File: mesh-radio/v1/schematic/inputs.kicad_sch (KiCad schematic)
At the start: 39 parts, among them J1 12401610E4#2A, J2 SM02B-SRSS-TB(LF)(SN), U1 TPS259470ARPWR, U2 TPS259470ARPWR, U3 TPS259470ARPWR

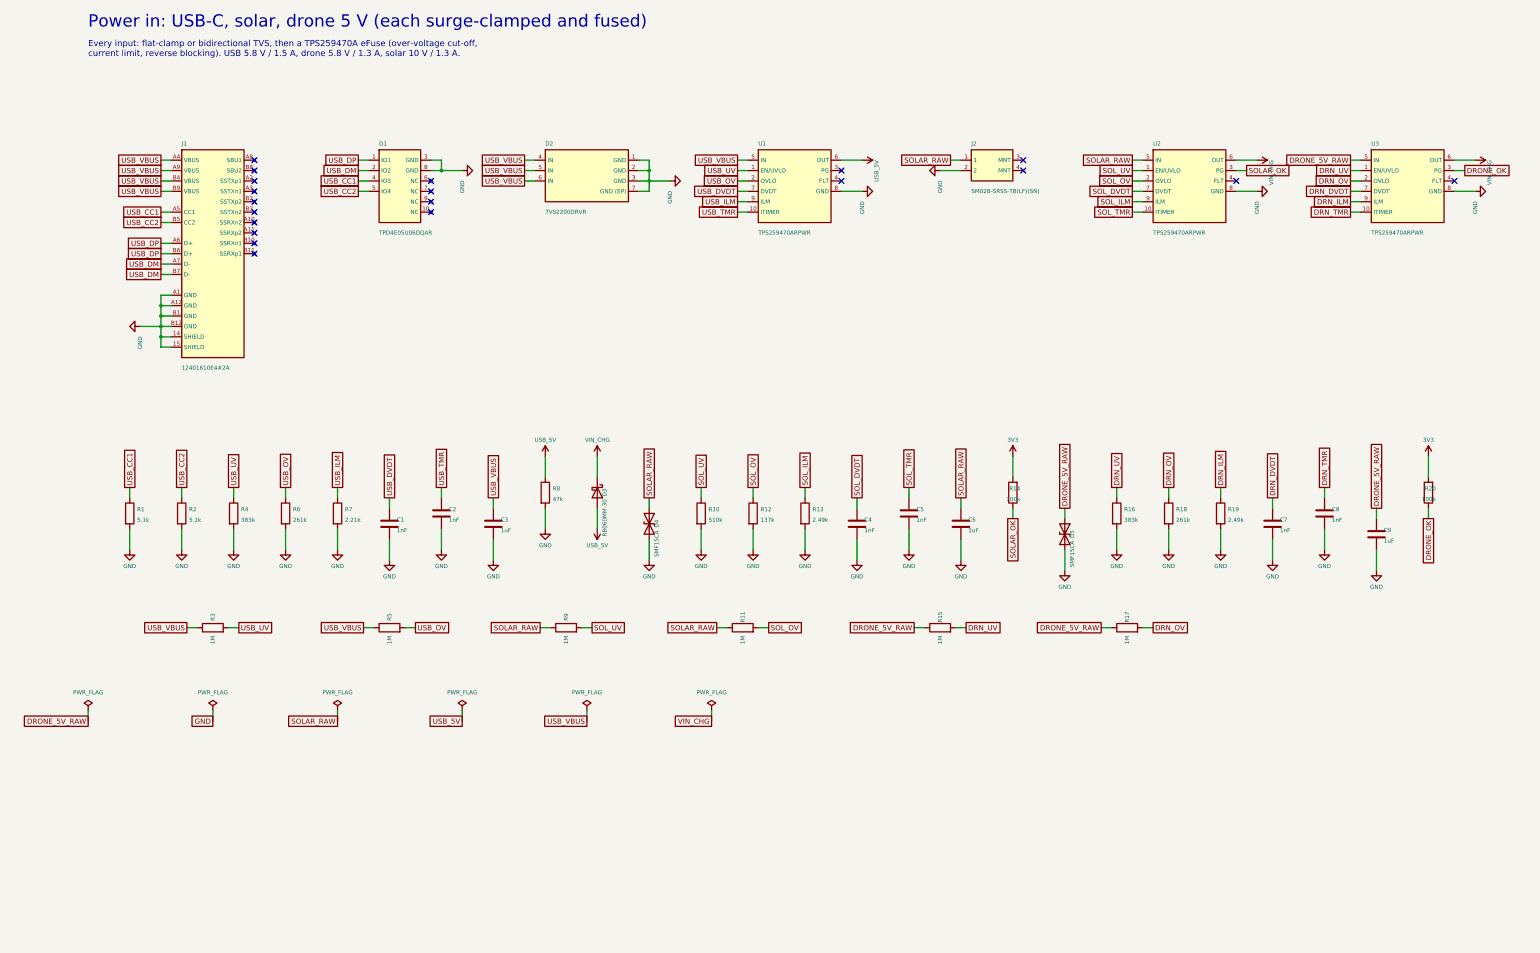
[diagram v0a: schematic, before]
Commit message: Mesh Radio v1: fix every design-review finding, add the part audit
An independent review of the schematic found two critical and nine further
issues; all are fixed in src/circuit.py:
- reverse-battery FET gate now returns to the cell's own minus terminal, so
  a backwards cell stays isolated even while USB/solar/drone power the board
- solar and drone inputs: reverse-blocking Schottky + 22 V flat-clamp TVS
  (the 15 V TVS would have failed on a 12 V panel); 4.7 V clamp on every
  eFuse EN/UVLO pin so 20 V on an input stays inside its rating
- ideal diode (LM66100) holds VSYS on the cell when a 3 W burst trips the
  charger's 3.0 V battery disconnect
- charge LED moved to STAT2 (charging), USB cut-off lowered to 5.4 V,
  charger /CE on a GPIO for firmware temperature control, -40 C TCXO,
  power mux on only with the amplifier, header VSYS pin removed
- firmware ceilings documented: SX1262 +20 dBm, amplifier 3.6 V by default

docs/part-audit.md: all 125 lines checked at DigiKey and LCSC (genuine
LCSC numbers, DigiKey numbers, second sources for out-of-stock lines);
parts cost about $76 at 10 boards, $58 at 100.

Schematic regenerated: ERC 0 violations, netlist equals circuit.py.

Co-Authored-By: Claude Opus 5.5 <noreply@anthropic.com>
Claude-Session: https://claude.ai/code/session_015TBB2ThqxHSgA8MkFosmn9
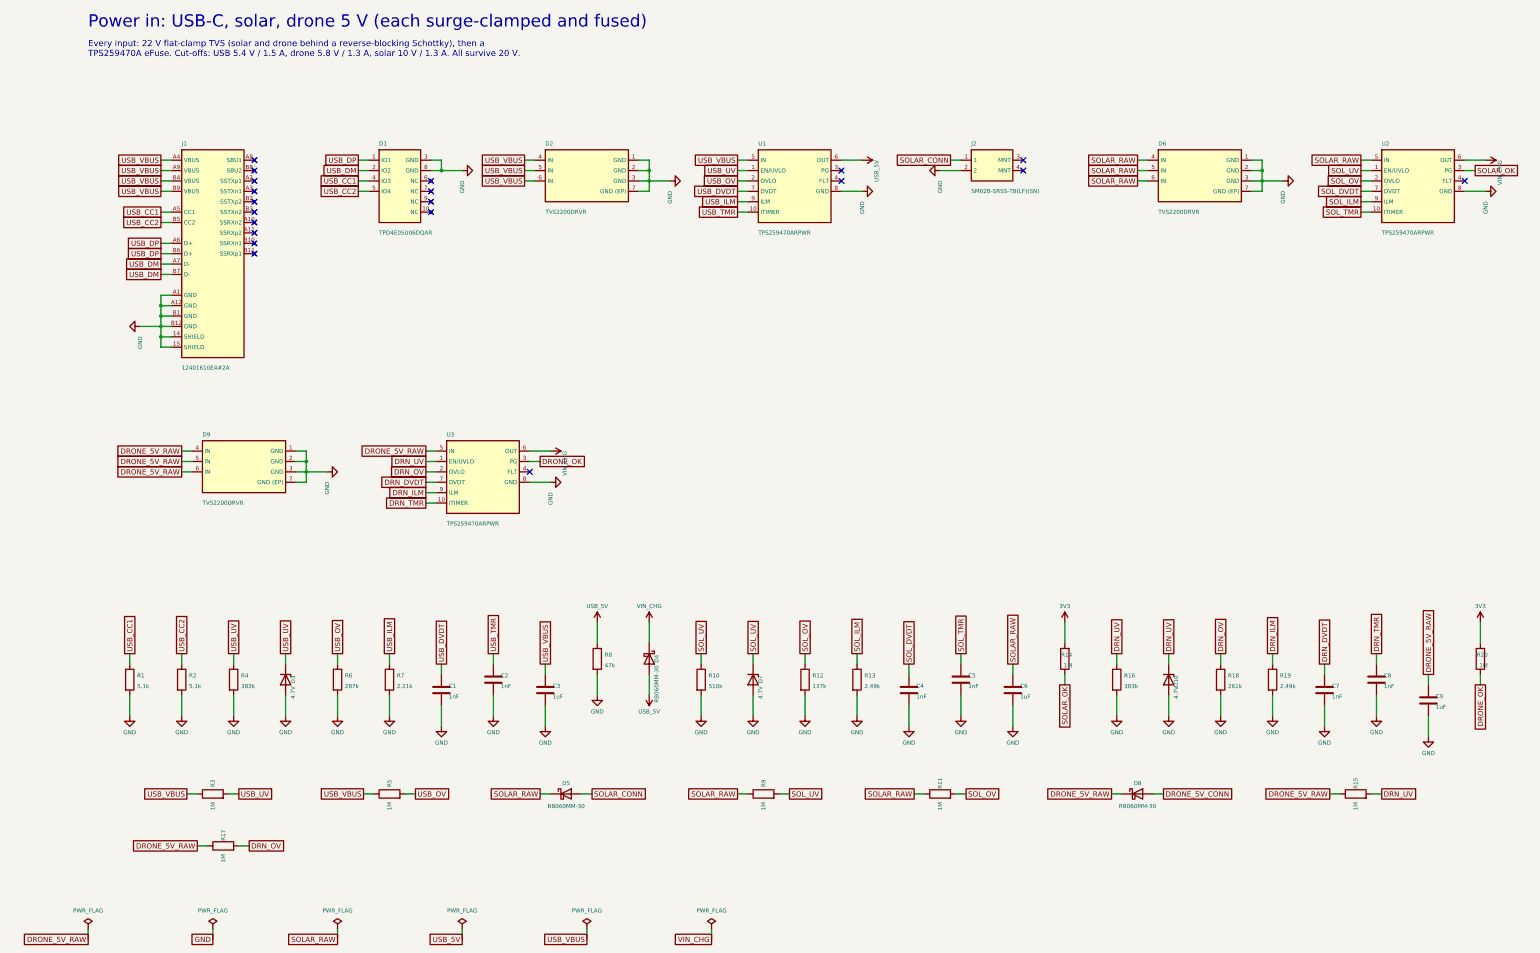
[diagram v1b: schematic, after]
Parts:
- added D10, D7: 4.7V, og:SOD-323FL, symbol og_device:D_Zener_ZENER4V7
- added D6, D9: TVS2200DRVR, og:WSON-6_L2.0-W2.0-P0.65-BL-EP, symbol og:TVS2200
- added D8: RB060MM-30, og:SOD-123FL, symbol og_device:D_Schottky_RB060MM
- C1, C2, C4, C5, C7, C8: DigiKey (none) -> 490-3244-1-ND
- C3, C6, C9: DigiKey (none) -> 1276-1184-1-ND
- D1: DigiKey (none) -> 296-35765-1-ND
- D2: DigiKey (none) -> 296-52187-1-ND
- D3: value RB060MM-30 -> 4.7V; footprint og:SOD-123FL -> og:SOD-323FL; symbol og_device:D_Schottky_RB060MM -> og_device:D_Zener_ZENER4V7; LCSC C308720 -> C209560; MPN RB060MM-30TR -> UDZVTE-174.7B
- D4, D5: value SMF15CA -> RB060MM-30; symbol og_device:D_TVS_SMF15CA -> og_device:D_Schottky_RB060MM; DigiKey (none) -> RB060MM-30CT-ND; LCSC C1851361 -> C308720; MPN SMF15CA -> RB060MM-30TR; Manufacturer Littelfuse -> Rohm
- J1: DigiKey (none) -> 12401610E4#2ACT-ND
- J2: DigiKey (none) -> 455-SM02B-SRSS-TBCT-ND
- R1, R2: DigiKey (none) -> 311-5.10KLRCT-ND
- R10: DigiKey (none) -> 311-510KLRCT-ND
- R11, R15, R17, R3, R5, R9: DigiKey (none) -> 311-1.00MLRCT-ND
- R12: DigiKey (none) -> YAG2972CT-ND
- R13, R19: DigiKey (none) -> 311-2.49KLRCT-ND
- R14, R20: value 100k -> 1M; DigiKey (none) -> 311-1.00MLRCT-ND; LCSC C60491 -> C138033; MPN RC0402FR-07100KL -> RC0402FR-071ML
- R16, R4: DigiKey (none) -> YAG3139CT-ND
- R18: DigiKey (none) -> 311-261KLRCT-ND
- R6: value 261k -> 287k; LCSC C185437 -> C327358; MPN RC0402FR-07261KL -> RC0402FR-07287KL
- R7: DigiKey (none) -> 311-2.21KLRCT-ND
- R8: DigiKey (none) -> 311-47.0KLRCT-ND
- U1, U2, U3: DigiKey (none) -> 296-TPS259470ARPWRCT-ND
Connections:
- net DRN_UV: now also D10.1 (K)
- net DRONE_5V_RAW: now also D8.1 (K), D9.4 (IN), D9.5 (IN), D9.6 (IN); no longer D5.1 (A1)
- net GND: now also D3.2 (A), D10.2 (A), D6.1 (GND), D6.2 (GND), D6.3 (GND), D6.7 (GND (EP)), D7.2 (A), D9.1 (GND), D9.2 (GND), D9.3 (GND), D9.7 (GND (EP)); no longer D4.2 (A2), D5.2 (A2)
- net SOLAR_RAW: now also D5.1 (K), D6.4 (IN), D6.5 (IN), D6.6 (IN); no longer D4.1 (A1), J2.1
- net SOL_UV: now also D7.1 (K)
- net USB_5V: now also D4.2 (A); no longer D3.2 (A)
- net USB_UV: now also D3.1 (K)
- net VIN_CHG: now also D4.1 (K); no longer D3.1 (K)
- new net DRONE_5V_CONN: D8.2 (A)
- new net SOLAR_CONN: D5.2 (A), J2.1
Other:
- note added: "Every input: 22 V flat-clamp TVS (solar and drone behind a reverse-blocking Schottky), then a TPS259470A eFuse. Cut-offs: USB 5.4 V / 1.5 A, drone 5.8 V / 1.3 A, solar 10 V / 1.3 A. All survive 20 V."
- note removed: "Every input: flat-clamp or bidirectional TVS, then a TPS259470A eFuse (over-voltage cut-off, current limit, reverse blocking). USB 5.8 V / 1.5 A, drone 5.8 V / 1.3 A, solar 10 V / 1.3 A."
- moved on the sheet: C1, C2, C3, C4, C5, C6, C7, C8, C9, D3, D4, D5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

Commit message: Mesh radio v1: power-path and firmware rework in progress (snapshot)
Co-Authored-By: Claude Opus 5.5 <noreply@anthropic.com>
Claude-Session: https://claude.ai/code/session_015TBB2ThqxHSgA8MkFosmn9
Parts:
- removed C9: 1uF, og:C_0603, symbol Device:C
- removed D10, D7: 4.7V, og:SOD-323FL, symbol og_device:D_Zener_ZENER4V7
- removed D8: RB060MM-30, og:SOD-123FL, symbol og_device:D_Schottky_RB060MM
- removed D9: TVS2200DRVR, og:WSON-6_L2.0-W2.0-P0.65-BL-EP, symbol og:TVS2200
- added R21: 1.5M, og:R_0402, symbol Device:R
- added R22: 100k, og:R_0402, symbol Device:R
- C1: value 1nF -> 100pF; DigiKey 490-3244-1-ND -> 490-5922-1-ND; LCSC C76947 -> C77177; MPN GRM1555C1H102JA01D -> GRM1555C1H101JA01D
- C3: value 1uF -> 1nF; footprint og:C_0603 -> og:C_0402; DigiKey 1276-1184-1-ND -> 490-3244-1-ND; LCSC C29936 -> C76947; MPN CL10B105KA8NNNC -> GRM1555C1H102JA01D; Manufacturer Samsung Electro-Mechanics -> Murata
- C4, C7, C8: value 1nF -> 1uF; footprint og:C_0402 -> og:C_0603; DigiKey 490-3244-1-ND -> 587-2400-1-ND; LCSC C76947 -> C92848; MPN GRM1555C1H102JA01D -> UMK107BJ105KA-T; Manufacturer Murata -> Taiyo Yuden
- C5: value 1nF -> 4.7uF; footprint og:C_0402 -> og:C_1206; DigiKey 490-3244-1-ND -> 1276-2789-1-ND; LCSC C76947 -> C51205; MPN GRM1555C1H102JA01D -> CL31B475KBHNNNE; Manufacturer Murata -> Samsung Electro-Mechanics
- C6: value 1uF -> 4.7uF; DigiKey 1276-1184-1-ND -> 1276-1044-1-ND; LCSC C29936 -> C1705; MPN CL10B105KA8NNNC -> CL10A475KP8NNNC
- D3: value 4.7V -> 5.6V; symbol og_device:D_Zener_ZENER4V7 -> og_device:D_Zener_ZENER5V6; DigiKey (none) -> UDZVTE-175.6BCT-ND; LCSC C209560 -> C79630; MPN UDZVTE-174.7B -> UDZVTE-175.6B
- D5: value RB060MM-30 -> SMF33CA; symbol og_device:D_Schottky_RB060MM -> Device:D_TVS; DigiKey RB060MM-30CT-ND -> 18-SMF33CACT-ND; LCSC C308720 -> C1851347; MPN RB060MM-30TR -> SMF33CA; Manufacturer Rohm -> Littelfuse
- D6: value TVS2200DRVR -> SMF33CA; footprint og:WSON-6_L2.0-W2.0-P0.65-BL-EP -> og:SOD-123FL; symbol og:TVS2200 -> Device:D_TVS; DigiKey 296-52187-1-ND -> 18-SMF33CACT-ND; LCSC C523793 -> C1851347; MPN TVS2200DRVR -> SMF33CA; Manufacturer Texas Instruments -> Littelfuse
- R10: value 510k -> 22R; DigiKey 311-510KLRCT-ND -> 311-22.0LRCT-ND; LCSC C137961 -> C114765; MPN RC0402FR-07510KL -> RC0402FR-0722RL
- R11, R15, R17: value 1M -> 1.5M; DigiKey 311-1.00MLRCT-ND -> 13-RC0402FR-071M5LCT-ND; LCSC C138033 -> C138034; MPN RC0402FR-071ML -> RC0402FR-071M5L
- R12: value 137k -> 267k; DigiKey YAG2972CT-ND -> YAG3079CT-ND; LCSC C138058 -> C327360; MPN RC0402FR-07137KL -> RC0402FR-07267KL
- R13, R19: value 2.49k -> 1M; DigiKey 311-2.49KLRCT-ND -> 311-1.00MLRCT-ND; LCSC C145071 -> C138033; MPN RC0402FR-072K49L -> RC0402FR-071ML
- R14, R20: value 1M -> 2.1k; DigiKey 311-1.00MLRCT-ND -> YAG3098CT-ND; LCSC C138033 -> C163473; MPN RC0402FR-071ML -> RC0402FR-072K1L
- R16: value 383k -> 100k; DigiKey YAG3139CT-ND -> 311-100KLRCT-ND; LCSC C163468 -> C60491; MPN RC0402FR-07383KL -> RC0402FR-07100KL
- R18: value 261k -> 267k; DigiKey 311-261KLRCT-ND -> YAG3079CT-ND; LCSC C185437 -> C327360; MPN RC0402FR-07261KL -> RC0402FR-07267KL
- R3: value 1M -> 20k; DigiKey 311-1.00MLRCT-ND -> 311-20.0KLRCT-ND; LCSC C138033 -> C93942; MPN RC0402FR-071ML -> RC0402FR-0720KL
- R4: value 383k -> 7.68k; DigiKey YAG3139CT-ND -> YAG3237CT-ND; LCSC C163468 -> C155695; MPN RC0402FR-07383KL -> RC0402FR-077K68L
- R8: value 47k -> 1R; footprint og:R_0402 -> og:R_0805; DigiKey 311-47.0KLRCT-ND -> 541-1.00TCT-ND; LCSC C93943 -> C313850; MPN RC0402FR-0747KL -> CRCW08051R00FKEAHP; Manufacturer Yageo -> Vishay Dale
- R9: value 1M -> 2.2k; DigiKey 311-1.00MLRCT-ND -> 311-2.20KLRCT-ND; LCSC C138033 -> C114762; MPN RC0402FR-071ML -> RC0402FR-072K2L
- U2, U3: value TPS259470ARPWR -> MAX17608ATC+T; footprint og:VQFN-10_L2.0-W2.0-P0.45-TL -> og:TDFN-12_L3.0-W3.0-P0.50-BL-EP; symbol og:TPS259470A -> og:MAX17608; DigiKey 296-TPS259470ARPWRCT-ND -> 175-MAX17608ATC+TCT-ND; LCSC C3662799 -> C2155884; MPN TPS259470ARPWR -> MAX17608ATC+T; Manufacturer Texas Instruments -> Analog Devices
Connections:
- net 3V3 is gone; now on net GND: R14.2, R20.2
- net DRN_OV: now also U3.3 (OVLO); no longer U3.2 (OVLO)
- net DRN_UV: now also R19.2, U3.4 (UVLO); no longer R15.2, R16.1, U3.1 (EN/UVLO)
- net DRONE_5V_CONN: now also C8.1, D6.1 (A1), R17.1, R19.1, U3.1 (IN), U3.2 (IN), R21.1
- net DRONE_OK: now also R21.2, R22.1; no longer R20.1, U3.3 (PG)
- net GND: now also D5.2 (A2), R9.2, U2.13 (GND (EP)), U2.6 (CLMODE), U2.7 (GND), U3.13 (GND (EP)), U3.6 (CLMODE), U3.7 (GND), R22.2; no longer C5.2, D6.1 (GND), D6.3 (GND), D6.7 (GND (EP)), R10.2, R13.2, R19.2, U2.8 (GND), U3.8 (GND)
- net SOLAR_CONN: now also C7.1, D5.1 (A1), R11.1, R13.1, R15.1, U2.1 (IN), U2.2 (IN); no longer D5.2 (A)
- net SOLAR_OK: now also R15.2, R16.1; no longer R14.1, U2.3 (PG)
- net SOL_OV: now also U2.3 (OVLO); no longer U2.2 (OVLO)
- net SOL_UV: now also R13.2, U2.4 (UVLO); no longer R10.1, R9.2, U2.1 (EN/UVLO)
- net USB_5V: now also R10.1, R9.1; no longer R8.1
- net USB_DVDT: now also C2.1; no longer C1.1
- net USB_OV: now also C1.1
- net USB_TMR: now also C3.1; no longer C2.1
- net USB_VBUS: now also C4.1, C5.1; no longer C3.1
- net VIN_CHG: now also U2.11 (OUT), U2.12 (OUT), U3.11 (OUT), U3.12 (OUT); no longer U2.6 (OUT), U3.6 (OUT)
- removed net DRN_DVDT: C7.1, U3.7 (DVDT)
- net DRN_ILM: no longer names the net of U3.9 (FLAG)
- net DRN_ILM: no longer R19.1
- net DRN_TMR: no longer names the net of U3.10 (UVOV)
- net DRN_TMR: no longer C8.1
- removed net DRONE_5V_RAW: R15.1, R17.1, U3.5 (IN)
- removed net SOLAR_RAW: C6.1, D5.1 (K), D6.4 (IN), D6.5 (IN), D6.6 (IN), R11.1, R9.1, U2.5 (IN)
- removed net SOL_DVDT: C4.1, U2.7 (DVDT)
- net SOL_ILM: no longer names the net of U2.9 (FLAG)
- net SOL_ILM: no longer R13.1
- net SOL_TMR: no longer names the net of U2.10 (UVOV)
- net SOL_TMR: no longer C5.1
- new net DRN_SETI: R20.1, U3.8 (SETI)
- new net NRF_VBUS: C6.1, R10.2
- new net SOL_SETI: R14.1, U2.8 (SETI)
- new net USB_SNB: C5.2, R8.1
- no-connect marks 20 -> 24
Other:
- note added: "USB: 22 V flat-clamp TVS, a 4.7 uF + 1 R snubber and a TPS259470A eFuse (cut-off 5.4 V, 1.5 A). Solar and drone: 33 V TVS and a 60 V MAX17608 (cut-off 10 V, 0.71 A, blocks -60 V and reverse current)."
- note removed: "Every input: 22 V flat-clamp TVS (solar and drone behind a reverse-blocking Schottky), then a TPS259470A eFuse. Cut-offs: USB 5.4 V / 1.5 A, drone 5.8 V / 1.3 A, solar 10 V / 1.3 A. All survive 20 V."
- moved on the sheet: C1, C2, C3, C4, C5, C6, C7, C8, D3, D4, D5, R1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

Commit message: Mesh Radio v1 schematic: regenerated (gate clamp, NTC part); ERC 0, netlist equal
Co-Authored-By: Claude Opus 5.5 <noreply@anthropic.com>
Claude-Session: https://claude.ai/code/session_015TBB2ThqxHSgA8MkFosmn9
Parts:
- R6: DigiKey (none) -> YAG3088CT-ND
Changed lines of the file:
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@@
+			)
+		)
+		(property "DigiKey" "YAG3088CT-ND"
+			(at 76.2 134.62 0)
+			(effects
+				(font
+					(size 1.27 1.27)
+				)
+				(hide yes)
 			)
 		)
